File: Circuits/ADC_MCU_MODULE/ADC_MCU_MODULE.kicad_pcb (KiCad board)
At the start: 2 copper layers, 78.2 x 110 mm, 37 parts, among them J1 Arduino_Nano_Header, P1 POWER, P2 BNC, P3 BNC, P4 BNC, P5 BNC, P6 BNC, P7 BNC, P8 BNC, P9 BNC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

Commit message: ADD: ADC/MCU Module Fabrication Files
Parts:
- added P10: TEMP_MODULE, w_conn_kk100:kk100_22-23-2061, F.Cu at (83.0, 88.5)
- moved G*** 48.6 mm to (130.8, 84.5)
- moved REF** 11.0 mm to (77.8, 97.2)
- moved REF** 6.78 mm to (145.0, 80.8)
- moved REF** 0.77 mm to (145.5, 191.8)
- moved REF** 0.75 mm to (72.8, 191.8)
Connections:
- J1 pad 11: (no net) -> ~CS
- J1 pad 14: (no net) -> MOSI
- J1 pad 15: (no net) -> MISO
- J1 pad 16: (no net) -> SCK
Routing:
- net ~CS: track 0.00 -> 70.4 mm, vias 0 -> 2
- net MISO: track 0.00 -> 64.8 mm
- net MOSI: track 0.00 -> 63.5 mm
- net SCK: track 0.00 -> 42.3 mm
- net +5V: track 255.5 -> 263.4 mm, vias 0 -> 2
- net SDA: track 99.1 -> 97.3 mm, vias 2 -> 4
- net SCL: track 108.3 -> 106.8 mm, vias 0 -> 2
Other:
- board size 78.2 x 110 mm -> 78.8 x 117.5 mm

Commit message: EDIT: ADC_MCU new schematic
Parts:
- added P11: V_AMP_1, w_conn_kk156:kk156_26-64-4050, F.Cu at (189.3, 101.8)
- added P12: V_AMP_2, w_conn_kk156:kk156_26-64-4050, F.Cu at (189.3, 119.6)
- added P13: V_AMP_3, w_conn_kk156:kk156_26-64-4050, F.Cu at (210.9, 101.8)
- P10: value TEMP_MODULE -> TEMP_MODULE_OUT
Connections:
- J1 pad 10: (no net) -> V2_b2
- J1 pad 12: (no net) -> V2_b1
- J1 pad 13: (no net) -> V2_b0
- J1 pad 19: (no net) -> V1_b0
- J1 pad 20: (no net) -> V1_b1
- J1 pad 21: (no net) -> V1_b2
- J1 pad 22: (no net) -> V1_b3
- J1 pad 29: (no net) -> GND
- J1 pad 5: (no net) -> V3_b3
- J1 pad 6: (no net) -> V3_b2
- J1 pad 7: (no net) -> V3_b1
- J1 pad 8: (no net) -> V3_b0
- J1 pad 9: (no net) -> V2_b3
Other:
- board size 78.8 x 117.5 mm -> 87.5 x 117.5 mm

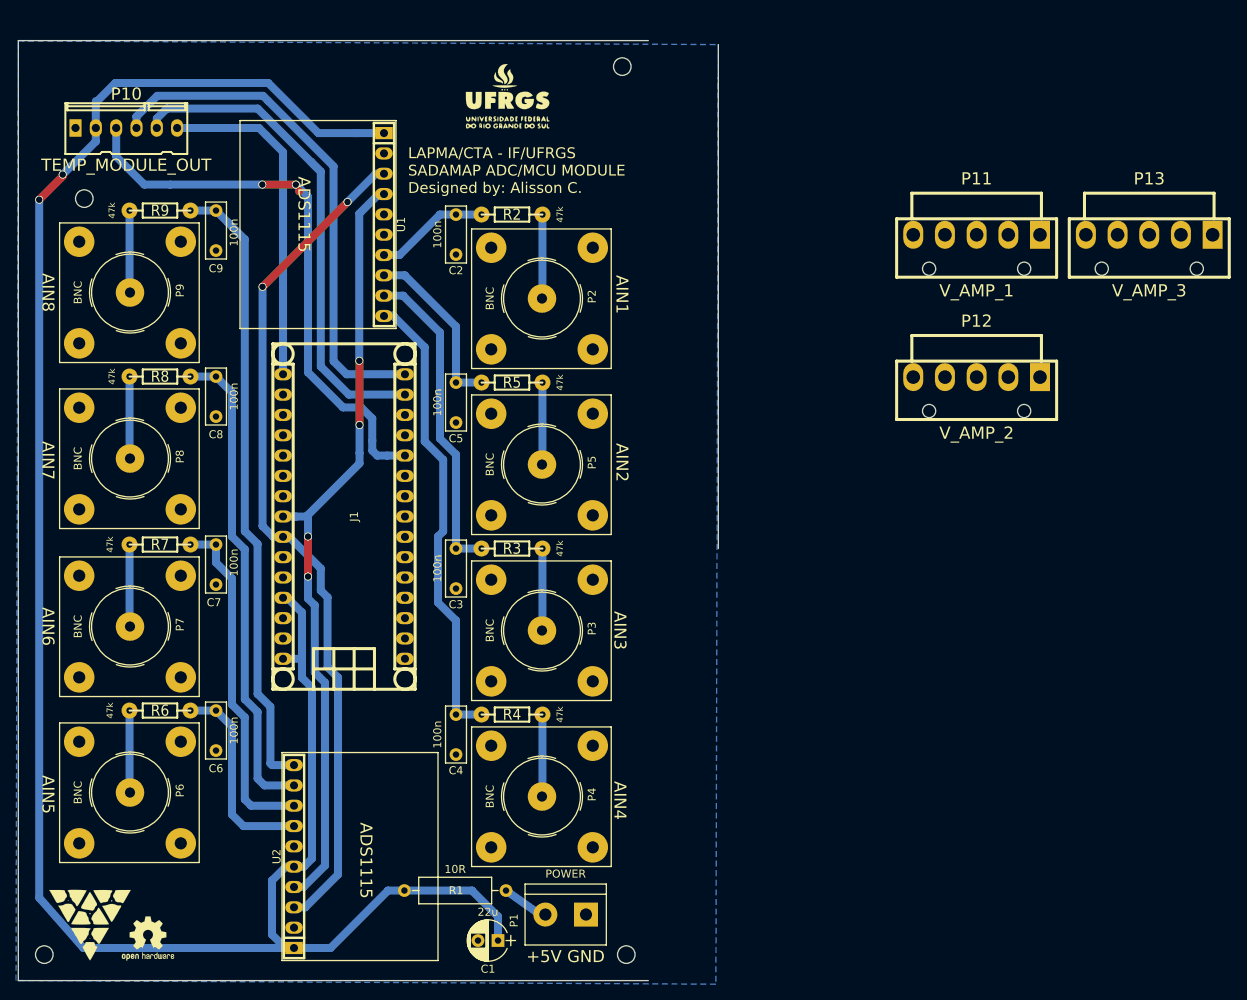
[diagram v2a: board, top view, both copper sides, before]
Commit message: ADD: ADC_MCU New Schematic
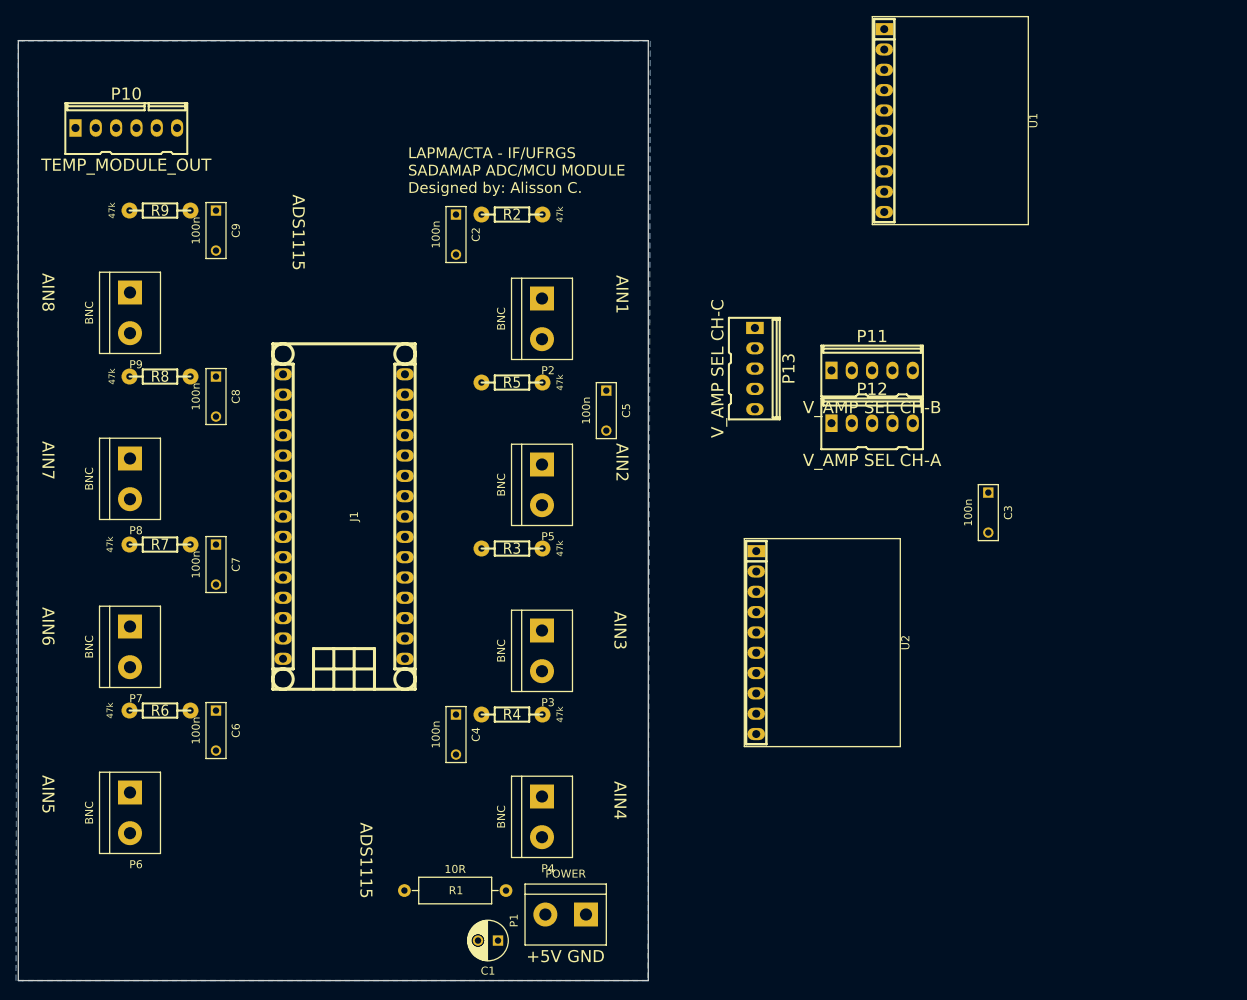
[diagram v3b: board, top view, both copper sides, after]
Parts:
- removed G***: LOGO, Symbols:ufrgs
- removed G***: LOGO, Symbols:cta
- removed REF** (x4): MountingHole_2.2mm_M2, Mounting_Holes:MountingHole_2.2mm_M2
- removed REF***: OSHW-Logo2_7.3x6mm_SilkScreen, Symbols:OSHW-Logo2_7.3x6mm_SilkScreen
- C1: footprint Capacitors_THT:CP_Radial_D5.0mm_P2.50mm -> Capacitors_ThroughHole:C_Radial_D5_L6_P2.5
- C2, C3, C4, C5, C6, C7, C8, C9: footprint Capacitors_THT:C_Rect_L7.0mm_W2.5mm_P5.00mm -> Capacitors_ThroughHole:C_Rect_L7_W2.5_P5
- J1: footprint Misc:arduino_nano_header -> w_conn_misc:arduino_nano_header
- P11: value V_AMP_1 -> V_AMP SEL CH-B; footprint w_conn_kk156:kk156_26-64-4050 -> w_conn_kk100:kk100_22-23-2051
- P12: value V_AMP_2 -> V_AMP SEL CH-A; footprint w_conn_kk156:kk156_26-64-4050 -> w_conn_kk100:kk100_22-23-2051
- P13: value V_AMP_3 -> V_AMP SEL CH-C; footprint w_conn_kk156:kk156_26-64-4050 -> w_conn_kk100:kk100_22-23-2051
- P2, P3, P4, P5, P6, P7, P8, P9: footprint Connectors:bnc-ci -> Connectors:bornier2
- moved U1 80.1 mm to (194.2, 87.5)
- moved U2 79.0 mm to (178.2, 152.8), turned to 270 degrees
- moved C3 66.9 mm to (190.8, 134.0)
- moved P13 52.1 mm to (161.5, 118.5), turned to 270 degrees
- moved P11 21.5 mm to (176.2, 118.8)
- moved C5 18.8 mm to (143.0, 121.2)
- moved P12 14.3 mm to (176.2, 125.4)
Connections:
- J1 pad 1: (no net) -> Net-(J1-Pad1)
- J1 pad 10: V2_b2 -> VC1
- J1 pad 11: ~CS -> VC2
- J1 pad 12: V2_b1 -> VC3
- J1 pad 13: V2_b0 -> ~CS
- J1 pad 17: (no net) -> Net-(J1-Pad17)
- J1 pad 18: (no net) -> Net-(J1-Pad18)
- J1 pad 19: V1_b0 -> VA0
- J1 pad 2: (no net) -> Net-(J1-Pad2)
- J1 pad 20: V1_b1 -> VA1
- J1 pad 21: V1_b2 -> VA2
- J1 pad 22: V1_b3 -> VA3
- J1 pad 25: (no net) -> Net-(J1-Pad25)
- J1 pad 26: (no net) -> Net-(J1-Pad26)
- J1 pad 28: (no net) -> Net-(J1-Pad28)
- J1 pad 3: (no net) -> Net-(J1-Pad3)
- J1 pad 5: V3_b3 -> VB0
- J1 pad 6: V3_b2 -> VB1
- J1 pad 7: V3_b1 -> VB2
- J1 pad 8: V3_b0 -> VB3
- J1 pad 9: V2_b3 -> VC0
- P11 pad 2: V1_b3 -> VB3
- P11 pad 3: V1_b2 -> VB2
- P11 pad 4: V1_b1 -> VB1
- P11 pad 5: V1_b0 -> VB0
- P12 pad 2: V2_b3 -> VA3
- P12 pad 3: V2_b2 -> VA2
- P12 pad 4: V2_b1 -> VA1
- P12 pad 5: V2_b0 -> VA0
- P13 pad 2: V3_b3 -> VC3
- P13 pad 3: V3_b2 -> VC2
- P13 pad 4: V3_b1 -> VC1
- P13 pad 5: V3_b0 -> VC0
- U1 pad 6: (no net) -> Net-(U1-Pad6)
- U2 pad 6: (no net) -> Net-(U2-Pad6)
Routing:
- net +5V: track 263.4 -> 0.00 mm, vias 2 -> 0
- net SCL: track 106.8 -> 0.00 mm, vias 2 -> 0
- net SDA: track 97.3 -> 0.00 mm, vias 4 -> 0
- net ADC8: track 78.2 -> 0.00 mm
- net ~CS: track 70.4 -> 0.00 mm, vias 2 -> 0
- net MISO: track 64.8 -> 0.00 mm
- net MOSI: track 63.5 -> 0.00 mm
- net ADC7: track 60.5 -> 0.00 mm
- net ADC4: track 58.2 -> 0.00 mm
- net ADC6: track 43.0 -> 0.00 mm
- net SCK: track 42.3 -> 0.00 mm
- net ADC3: track 39.9 -> 0.00 mm
- net ADC5: track 25.4 -> 0.00 mm
- net ADC2: track 21.8 -> 0.00 mm
- net ADC1: track 14.3 -> 0.00 mm
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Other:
- board size 87.5 x 117.5 mm -> 78.8 x 117.5 mm
